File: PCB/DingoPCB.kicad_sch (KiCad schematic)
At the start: 23 parts, among them J1 BATT(~15V), J10 BATT CHECK, J11 1935776, J12 1935776, J13 1935776, J14 1935776, J15 TEMP1, J16 TEMP2, J17 TEMP3, J18 TEMP4, J19 FAN1, J2 PWR1, J20 FAN2, J3 PWR2, J4 PWR3, J5 PWR4, J6 12VIN, J7 5VIN, J8 1935776, J9 1935776

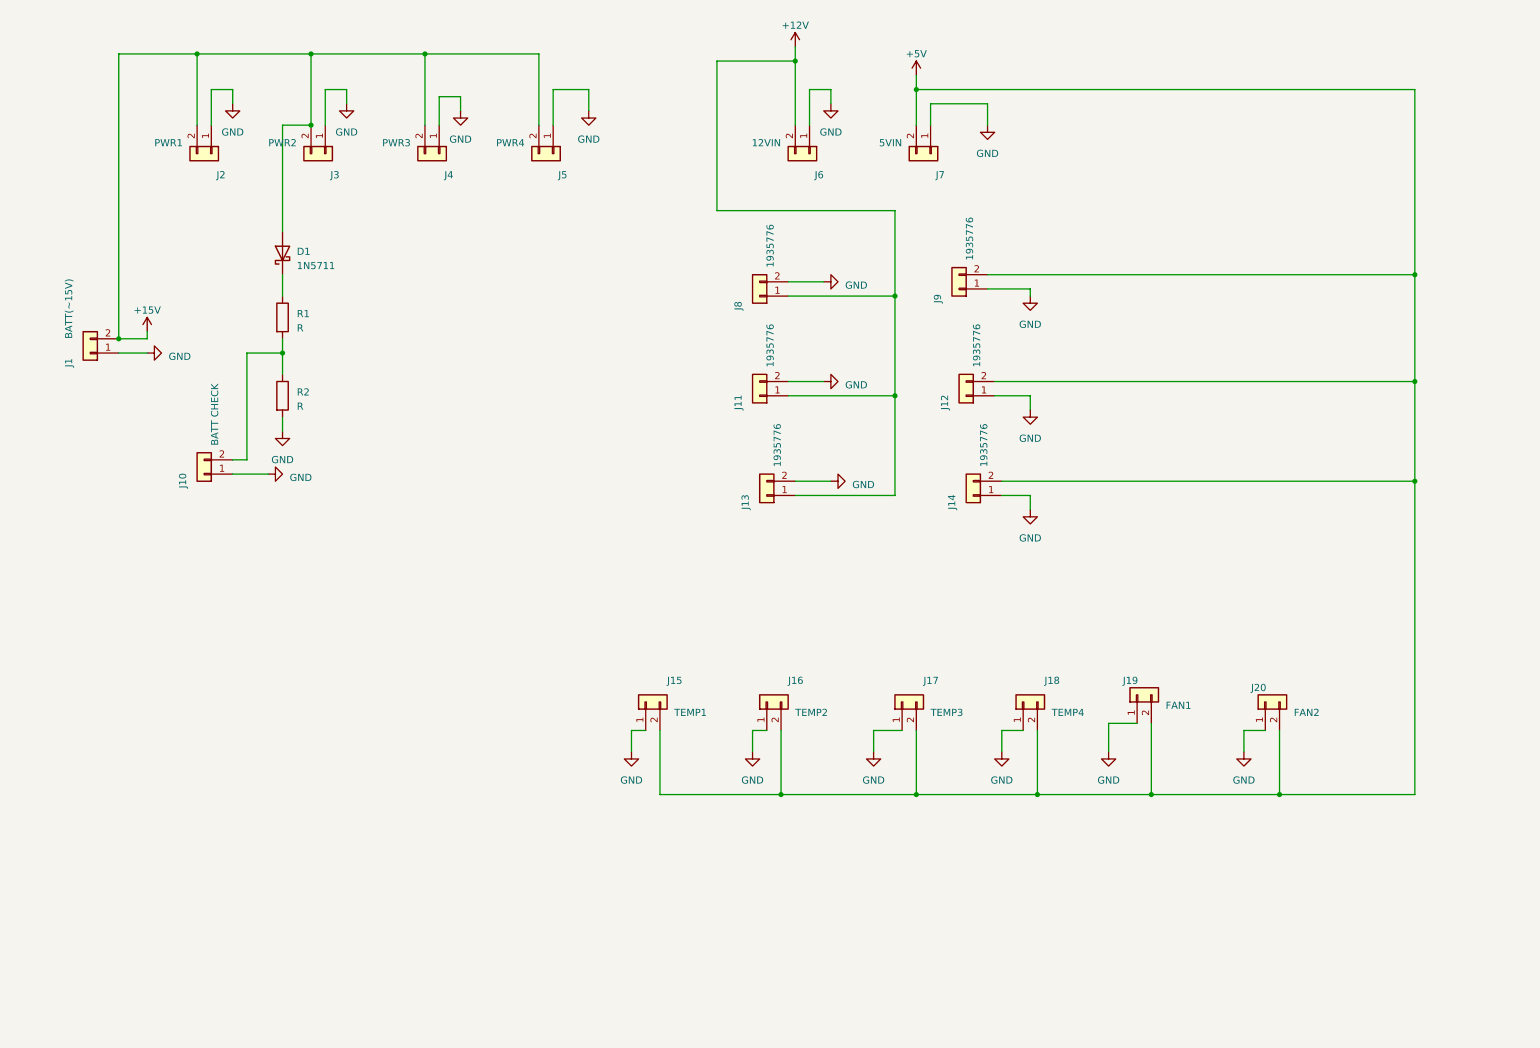
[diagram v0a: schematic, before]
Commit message: Adding updated servo carriers
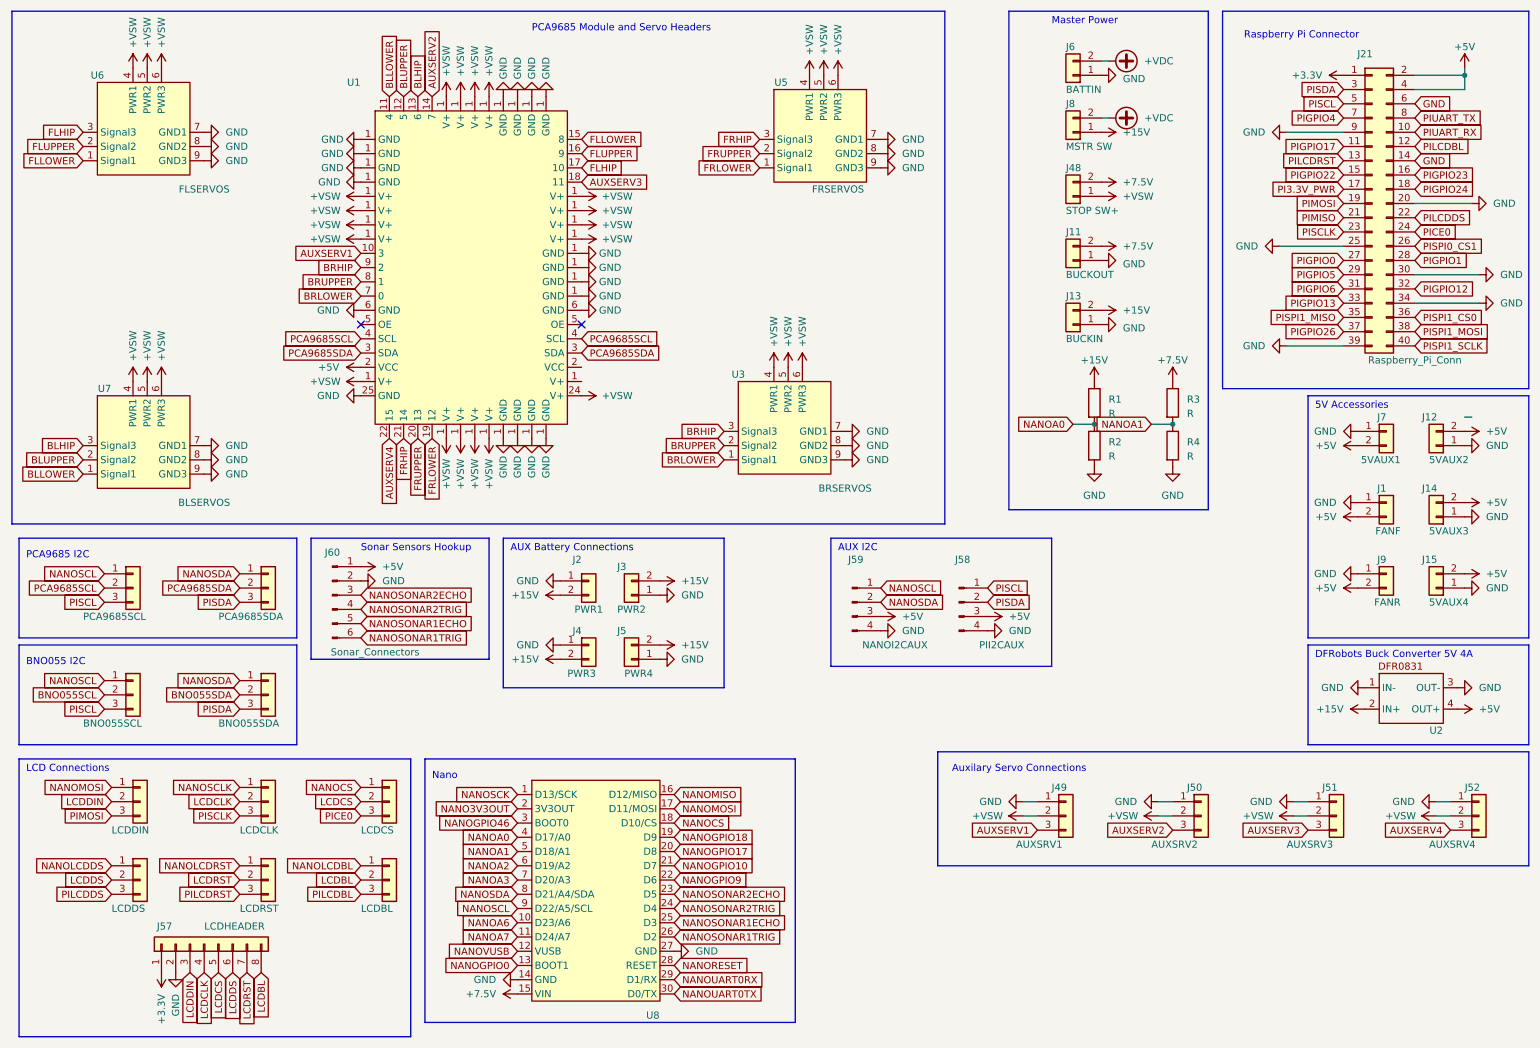
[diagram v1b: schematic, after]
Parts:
- removed D1: 1N5711, Diode_THT:D_DO-35_SOD27_P7.62mm_Horizontal, symbol Diode:1N5711
- removed J10: BATT CHECK, TerminalBlock_Phoenix:TerminalBlock_Phoenix_MKDS-1,5-2-5.08_1x02_P5.08mm_Horizontal, symbol Connector_Generic:Conn_01x02
- removed J16: TEMP2, Connector_JST:JST_EH_B2B-EH-A_1x02_P2.50mm_Vertical, symbol Connector_Generic:Conn_01x02
- removed J17: TEMP3, Connector_JST:JST_EH_B2B-EH-A_1x02_P2.50mm_Vertical, symbol Connector_Generic:Conn_01x02
- removed J18: TEMP4, Connector_JST:JST_EH_B2B-EH-A_1x02_P2.50mm_Vertical, symbol Connector_Generic:Conn_01x02
- removed J19: FAN1, Connector_JST:JST_EH_B2B-EH-A_1x02_P2.50mm_Vertical, symbol Connector_Generic:Conn_01x02
- removed J20: FAN2, Connector_JST:JST_EH_B2B-EH-A_1x02_P2.50mm_Vertical, symbol Connector_Generic:Conn_01x02
- added J10: PCA9685SDA, Connector_PinHeader_2.54mm:PinHeader_1x03_P2.54mm_Vertical, symbol Connector_Generic:Conn_01x03
- added J16: BNO055SDA, Connector_PinHeader_2.54mm:PinHeader_1x03_P2.54mm_Vertical, symbol Connector_Generic:Conn_01x03
- added J17: BNO055SCL, Connector_PinHeader_2.54mm:PinHeader_1x03_P2.54mm_Vertical, symbol Connector_Generic:Conn_01x03
- added J18: LCDDS, Connector_PinHeader_2.54mm:PinHeader_1x03_P2.54mm_Vertical, symbol Connector_Generic:Conn_01x03
- added J19: LCDRST, Connector_PinHeader_2.54mm:PinHeader_1x03_P2.54mm_Vertical, symbol Connector_Generic:Conn_01x03
- added J20: LCDBL, Connector_PinHeader_2.54mm:PinHeader_1x03_P2.54mm_Vertical, symbol Connector_Generic:Conn_01x03
- added J21: Raspberry_Pi_Conn, Connector_PinHeader_2.54mm:PinHeader_2x20_P2.54mm_Vertical, symbol Connector_Generic:Conn_02x20_Odd_Even
- added J48: STOP SW+, TerminalBlock_Phoenix:TerminalBlock_Phoenix_MKDS-1,5-2-5.08_1x02_P5.08mm_Horizontal, symbol Connector_Generic:Conn_01x02
- added J49: AUXSRV1, Connector_PinHeader_2.54mm:PinHeader_1x03_P2.54mm_Vertical, symbol Connector_Generic:Conn_01x03
- added J50: AUXSRV2, Connector_PinHeader_2.54mm:PinHeader_1x03_P2.54mm_Vertical, symbol Connector_Generic:Conn_01x03
- added J51: AUXSRV3, Connector_PinHeader_2.54mm:PinHeader_1x03_P2.54mm_Vertical, symbol Connector_Generic:Conn_01x03
- added J52: AUXSRV4, Connector_PinHeader_2.54mm:PinHeader_1x03_P2.54mm_Vertical, symbol Connector_Generic:Conn_01x03
- added J53: PCA9685SCL, Connector_PinHeader_2.54mm:PinHeader_1x03_P2.54mm_Vertical, symbol Connector_Generic:Conn_01x03
- added J54: LCDDIN, Connector_PinHeader_2.54mm:PinHeader_1x03_P2.54mm_Vertical, symbol Connector_Generic:Conn_01x03
- added J55: LCDCLK, Connector_PinHeader_2.54mm:PinHeader_1x03_P2.54mm_Vertical, symbol Connector_Generic:Conn_01x03
- added J56: LCDCS, Connector_PinHeader_2.54mm:PinHeader_1x03_P2.54mm_Vertical, symbol Connector_Generic:Conn_01x03
- added J57: LCDHEADER, Connector_PinHeader_2.54mm:PinHeader_1x08_P2.54mm_Horizontal, symbol Connector_Generic:Conn_01x08
- added J58: PII2CAUX, Connector_JST:JST_EH_B4B-EH-A_1x04_P2.50mm_Vertical, symbol Connector:Conn_01x04_Pin
- added J59: NANOI2CAUX, Connector_JST:JST_EH_B4B-EH-A_1x04_P2.50mm_Vertical, symbol Connector:Conn_01x04_Pin
- added J60: Sonar_Connectors, Connector_JST:JST_EH_B6B-EH-A_1x06_P2.50mm_Vertical, symbol Connector:Conn_01x06_Pin
- added R3, R4: R, Resistor_THT:R_Axial_DIN0204_L3.6mm_D1.6mm_P2.54mm_Vertical, symbol Device:R
- added U1: ~, PCA9685:Adafruit PCA9685 rev C, symbol Motor:AdaPCA9685
- added U2: ~, Inductor_THT:DFR0831, symbol Power_Management:DFR0831
- added U3: BRSERVOS, Connector:Three_Servo_Footprint, symbol Connector:Three_Servo_Connector
- added U5: FRSERVOS, Connector:Three_Servo_Footprint, symbol Connector:Three_Servo_Connector
- added U6: FLSERVOS, Connector:Three_Servo_Footprint, symbol Connector:Three_Servo_Connector
- added U7: BLSERVOS, Connector:Three_Servo_Footprint, symbol Connector:Three_Servo_Connector
- added U8: ~, Module:Arduino_Nano_ESP32, symbol MCU_Espressif:NANO_ESP32
- J1: value BATT(~15V) -> FANF; footprint TerminalBlock_Phoenix:TerminalBlock_Phoenix_MKDS-1,5-2-5.08_1x02_P5.08mm_Horizontal -> Connector_JST:JST_EH_B2B-EH-A_1x02_P2.50mm_Vertical
- J11: value 1935776 -> BUCKOUT; footprint Connector_JST:JST_EH_B2B-EH-A_1x02_P2.50mm_Vertical -> TerminalBlock_Phoenix:TerminalBlock_Phoenix_MKDS-1,5-2-5.08_1x02_P5.08mm_Horizontal
- J12: value 1935776 -> 5VAUX2
- J13: value 1935776 -> BUCKIN; footprint Connector_JST:JST_EH_B2B-EH-A_1x02_P2.50mm_Vertical -> TerminalBlock_Phoenix:TerminalBlock_Phoenix_MKDS-1,5-2-5.08_1x02_P5.08mm_Horizontal
- J14: value 1935776 -> 5VAUX3
- J15: value TEMP1 -> 5VAUX4
- J6: value 12VIN -> BATTIN
- J7: value 5VIN -> 5VAUX1; footprint TerminalBlock_Phoenix:TerminalBlock_Phoenix_MKDS-1,5-2-5.08_1x02_P5.08mm_Horizontal -> Connector_JST:JST_EH_B2B-EH-A_1x02_P2.50mm_Vertical
- J8: value 1935776 -> MSTR SW; footprint Connector_JST:JST_EH_B2B-EH-A_1x02_P2.50mm_Vertical -> TerminalBlock_Phoenix:TerminalBlock_Phoenix_MKDS-1,5-2-5.08_1x02_P5.08mm_Horizontal
- J9: value 1935776 -> FANR
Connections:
- net +15V: now also J13.2 (Pin_2), J8.1 (Pin_1), R1.1, U2.2 (IN+); no longer J1.2 (Pin_2)
- net +5V: now also J1.2 (Pin_2), J21.2 (Pin_2), J21.4 (Pin_4), J58.3 (Pin_3), J59.3 (Pin_3), J60.1 (Pin_1), U1.2 (VCC), U2.4 (OUT+)
- net GND: now also J11.1 (Pin_1), J13.1 (Pin_1), J21.14 (Pin_14), J21.20 (Pin_20), J21.25 (Pin_25), J21.30 (Pin_30), J21.34 (Pin_34), J21.39 (Pin_39), J21.6 (Pin_6), J21.9 (Pin_9), J49.1 (Pin_1), J50.1 (Pin_1), J51.1 (Pin_1), J52.1 (Pin_1), J57.2 (Pin_2), J58.4 (Pin_4), J59.4 (Pin_4), J60.2 (Pin_2), R4.2, U1.1 (V+), U1.25 (GND), U1.6 (GND), U2.1 (IN-), U2.3 (OUT-), U3.7 (GND1), U3.8 (GND2), U3.9 (GND3), U5.7 (GND1), U5.8 (GND2), U5.9 (GND3), U6.7 (GND1), U6.8 (GND2), U6.9 (GND3), U7.7 (GND1), U7.8 (GND2), U7.9 (GND3), U8.14 (GND), U8.27 (GND); no longer J11.2 (Pin_2), J13.2 (Pin_2), J8.2 (Pin_2)
- net NANOA0: now reaches R1.2, R2.1
- net NANOA0: now also U8.4 (D17/A0)
- removed net +12V: J11.1 (Pin_1), J13.1 (Pin_1), J6.2 (Pin_2), J8.1 (Pin_1)
- new net +3.3V: J21.1 (Pin_1), J57.1 (Pin_1)
- new net +7.5V: J11.2 (Pin_2), J48.2 (Pin_2), R3.1, U8.15 (VIN)
- new net +VDC: J6.2 (Pin_2), J8.2 (Pin_2)
- new net +VSW: J48.1 (Pin_1), J49.2 (Pin_2), J50.2 (Pin_2), J51.2 (Pin_2), J52.2 (Pin_2), U1.1 (V+), U1.24 (V+), U3.4 (PWR1), U3.5 (PWR2), U3.6 (PWR3), U5.4 (PWR1), U5.5 (PWR2), U5.6 (PWR3), U6.4 (PWR1), U6.5 (PWR2), U6.6 (PWR3), U7.4 (PWR1), U7.5 (PWR2), U7.6 (PWR3)
- new net AUXSERV1: J49.3 (Pin_3), U1.10 (3)
- new net AUXSERV2: J50.3 (Pin_3), U1.14 (7)
- new net AUXSERV3: J51.3 (Pin_3), U1.18 (11)
- new net AUXSERV4: J52.3 (Pin_3), U1.22 (15)
- new net BLHIP: U1.13 (6), U7.3 (Signal3)
- new net BLLOWER: U1.11 (4), U7.1 (Signal1)
- new net BLUPPER: U1.12 (5), U7.2 (Signal2)
- new net BNO055SCL: J17.2 (Pin_2)
- new net BNO055SDA: J16.2 (Pin_2)
- new net BRHIP: U1.9 (2), U3.3 (Signal3)
- new net BRLOWER: U1.7 (0), U3.1 (Signal1)
- new net BRUPPER: U1.8 (1), U3.2 (Signal2)
- new net FLHIP: U1.17 (10), U6.3 (Signal3)
- new net FLLOWER: U1.15 (8), U6.1 (Signal1)
- new net FLUPPER: U1.16 (9), U6.2 (Signal2)
- new net FRHIP: U1.21 (14), U5.3 (Signal3)
- new net FRLOWER: U1.19 (12), U5.1 (Signal1)
- new net FRUPPER: U1.20 (13), U5.2 (Signal2)
- new net LCDBL: J20.2 (Pin_2), J57.8 (Pin_8)
- new net LCDCLK: J55.2 (Pin_2), J57.4 (Pin_4)
- new net LCDCS: J56.2 (Pin_2), J57.5 (Pin_5)
- new net LCDDIN: J54.2 (Pin_2), J57.3 (Pin_3)
- new net LCDDS: J18.2 (Pin_2), J57.6 (Pin_6)
- new net LCDRST: J19.2 (Pin_2), J57.7 (Pin_7)
- new net NANO3V3OUT: U8.2 (3V3OUT)
- new net NANOA1: R3.2, R4.1, U8.5 (D18/A1)
- new net NANOA2: U8.6 (D19/A2)
- new net NANOA3: U8.7 (D20/A3)
- new net NANOA6: U8.10 (D23/A6)
- new net NANOA7: U8.11 (D24/A7)
- new net NANOCS: J56.1 (Pin_1), U8.18 (D10/CS)
- new net NANOGPIO0: U8.13 (BOOT1)
- new net NANOGPIO10: U8.21 (D7)
- new net NANOGPIO17: U8.20 (D8)
- new net NANOGPIO18: U8.19 (D9)
- new net NANOGPIO46: U8.3 (BOOT0)
- new net NANOGPIO9: U8.22 (D6)
- new net NANOLCDBL: J20.1 (Pin_1)
- new net NANOLCDDS: J18.1 (Pin_1)
- new net NANOLCDRST: J19.1 (Pin_1)
- new net NANOMISO: U8.16 (D12/MISO)
- new net NANOMOSI: J54.1 (Pin_1), U8.17 (D11/MOSI)
- new net NANORESET: U8.28 (RESET)
- new net NANOSCK: U8.1 (D13/SCK)
- new net NANOSCL: J17.1 (Pin_1), J53.1 (Pin_1), J59.1 (Pin_1), U8.9 (D22/A5/SCL)
- new net NANOSCLK: J55.1 (Pin_1)
- new net NANOSDA: J10.1 (Pin_1), J16.1 (Pin_1), J59.2 (Pin_2), U8.8 (D21/A4/SDA)
- new net NANOSONAR1ECHO: J60.5 (Pin_5), U8.25 (D3)
- new net NANOSONAR1TRIG: J60.6 (Pin_6), U8.26 (D2)
- new net NANOSONAR2ECHO: J60.3 (Pin_3), U8.23 (D5)
- new net NANOSONAR2TRIG: J60.4 (Pin_4), U8.24 (D4)
- new net NANOUART0RX: U8.29 (D1/RX)
- new net NANOUART0TX: U8.30 (D0/TX)
- new net NANOVUSB: U8.12 (VUSB)
- new net PCA9685SCL: J53.2 (Pin_2), U1.4 (SCL)
- new net PCA9685SDA: J10.2 (Pin_2), U1.3 (SDA)
- new net PI3.3V_PWR: J21.17 (Pin_17)
- new net PICE0: J21.24 (Pin_24), J56.3 (Pin_3)
- new net PIGPIO0: J21.27 (Pin_27)
- new net PIGPIO1: J21.28 (Pin_28)
- new net PIGPIO12: J21.32 (Pin_32)
- new net PIGPIO13: J21.33 (Pin_33)
- new net PIGPIO17: J21.11 (Pin_11)
- new net PIGPIO22: J21.15 (Pin_15)
- new net PIGPIO23: J21.16 (Pin_16)
- new net PIGPIO24: J21.18 (Pin_18)
- new net PIGPIO26: J21.37 (Pin_37)
- new net PIGPIO4: J21.7 (Pin_7)
- new net PIGPIO5: J21.29 (Pin_29)
- new net PIGPIO6: J21.31 (Pin_31)
- new net PILCDBL: J20.3 (Pin_3), J21.12 (Pin_12)
- new net PILCDDS: J18.3 (Pin_3), J21.22 (Pin_22)
- new net PILCDRST: J19.3 (Pin_3), J21.13 (Pin_13)
- new net PIMISO: J21.21 (Pin_21)
- new net PIMOSI: J21.19 (Pin_19), J54.3 (Pin_3)
- new net PISCL: J17.3 (Pin_3), J21.5 (Pin_5), J53.3 (Pin_3), J58.1 (Pin_1)
- new net PISCLK: J21.23 (Pin_23), J55.3 (Pin_3)
- new net PISDA: J10.3 (Pin_3), J16.3 (Pin_3), J21.3 (Pin_3), J58.2 (Pin_2)
- new net PISPI0_CS1: J21.26 (Pin_26)
- new net PISPI1_CS0: J21.36 (Pin_36)
- new net PISPI1_MISO: J21.35 (Pin_35)
- new net PISPI1_MOSI: J21.38 (Pin_38)
- new net PISPI1_SCLK: J21.40 (Pin_40)
- new net PIUART_RX: J21.10 (Pin_10)
- new net PIUART_TX: J21.8 (Pin_8)
- no-connect marks 0 -> 2
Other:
- note added: "5V Accessories"
- note added: "AUX Battery Connections"
- note added: "AUX I2C"
- note added: "Auxilary Servo Connections"
- note added: "BNO055 I2C"
- note added: "DFRobots Buck Converter 5V 4A"
- note added: "LCD Connections"
- note added: "Master Power"
- note added: "Nano"
- note added: "PCA9685 I2C"
- note added: "PCA9685 Module and Servo Headers"
- note added: "Raspberry Pi Connector"
- note added: "Sonar Sensors Hookup"
- moved on the sheet: J2, J3, J4, J5, J7, R1, R2
